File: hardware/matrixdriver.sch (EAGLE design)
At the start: 50 parts, among them IC1 75176AD, IC2 4017D, IC3 ULN2803, IC4 7805DT, Q1 20MHZ, Q2 MMBT4403LT1SMD, Q3 BC856, Q4 BC856, Q5 BC856, Q6 BC856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

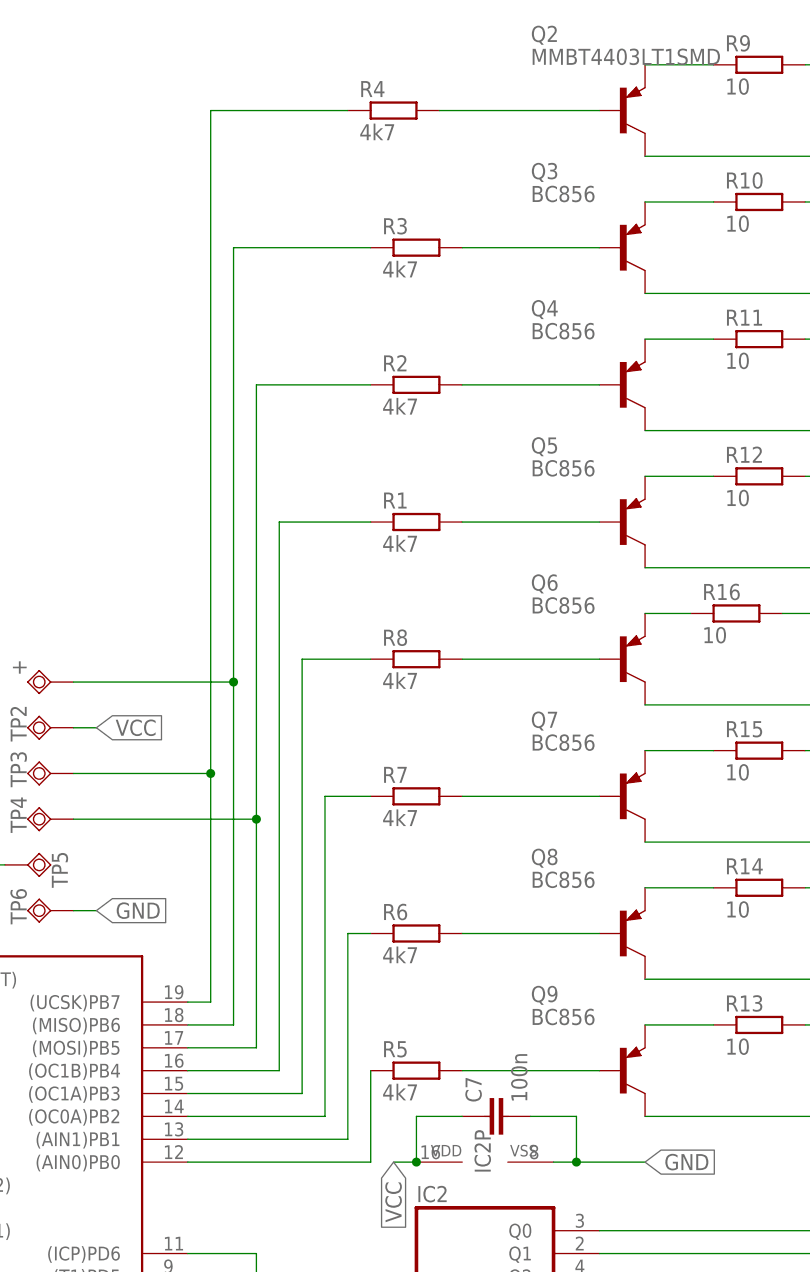
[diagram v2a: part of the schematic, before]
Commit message: board changes without resistor at base
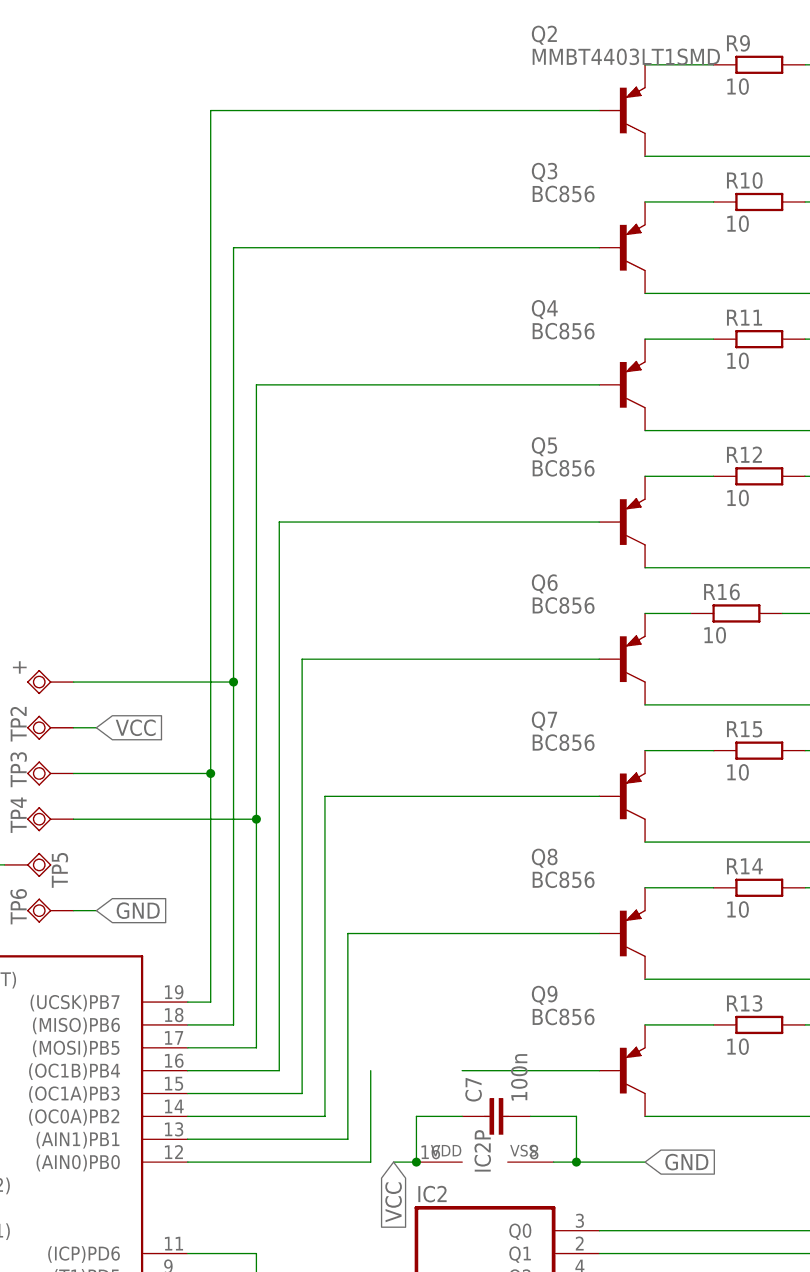
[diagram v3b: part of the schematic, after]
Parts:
- removed R1, R2, R3, R4, R5, R6, R7, R8: 4k7, resistor:R-EU_R1206
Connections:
- removed net N$37: Q2.B, R4.2
- removed net N$38: Q4.B, R2.2
- removed net N$39: Q5.B, R1.2
- removed net N$40: Q8.B, R6.2
- removed net N$42: Q6.B, R8.2
- removed net N$43: Q7.B, R7.2
- removed net N$7: +.TP, R3.1, U$1.(MISO)PB6
- net N$1: no longer R5.1
- net N$2: now also Q8.B; no longer R6.1
- net N$3: now also Q7.B; no longer R7.1
- net N$32: now also +.TP, U$1.(MISO)PB6; no longer R3.2
- net N$4: now also Q6.B; no longer R8.1
- net N$41: no longer R5.2
- net N$5: now also Q5.B; no longer R1.1
- net N$6: now also Q4.B; no longer R2.1
- net N$8: now also Q2.B; no longer R4.1
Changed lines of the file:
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@@
 <part name="Q1" library="crystal" deviceset="CRYSTAL" device="HC49UP" value="20MHZ"/>
 <part name="U$2" library="con-dc-jack" deviceset="CUI_PJ-102A" device=""/>
-<part name="R2" library="resistor" deviceset="R-EU_" device="R1206" value="4k7"/>
-<part name="R1" library="resistor" deviceset="R-EU_" device="R1206" value="4k7"/>
-<part name="R3" library="resistor" deviceset="R-EU_" device="R1206" value="4k7"/>
-<part name="R4" library="resistor" deviceset="R-EU_" device="R1206" value="4k7"/>
-<part name="R5" library="resistor" deviceset="R-EU_" device="R1206" value="4k7"/>
-<part name="R6" library="resistor" deviceset="R-EU_" device="R1206" value="4k7"/>
-<part name="R7" library="resistor" deviceset="R-EU_" device="R1206" value="4k7"/>
-<part name="R8" library="resistor" deviceset="R-EU_" device="R1206" value="4k7"/>
 <part name="R9" library="resistor" deviceset="R-EU_" device="R1206" value="10"/>
 <part name="R10" library="resistor" deviceset="R-EU_" device="R1206" value="10"/>
@@
 <instance part="Q1" gate="G$1" x="30.48" y="68.58" rot="R90"/>
 <instance part="U$2" gate="G$1" x="12.7" y="101.6" rot="R270"/>
-<instance part="R2" gate="G$1" x="101.6" y="160.02"/>
-<instance part="R1" gate="G$1" x="101.6" y="144.78"/>
-<instance part="R3" gate="G$1" x="101.6" y="175.26"/>
-<instance part="R4" gate="G$1" x="99.06" y="190.5"/>
-<instance part="R5" gate="G$1" x="101.6" y="83.82"/>
-<instance part="R6" gate="G$1" x="101.6" y="99.06"/>
-<instance part="R7" gate="G$1" x="101.6" y="114.3"/>
-<instance part="R8" gate="G$1" x="101.6" y="129.54"/>
 <instance part="R9" gate="G$1" x="139.7" y="195.58"/>
 <instance part="R10" gate="G$1" x="139.7" y="180.34"/>
@@
 <wire x1="76.2" y1="73.66" x2="96.52" y2="73.66" width="0.1524" layer="91"/>
 <wire x1="96.52" y1="73.66" x2="96.52" y2="83.82" width="0.1524" layer="91"/>
-<pinref part="R5" gate="G$1" pin="1"/>
 </segment>
 </net>
@@
 <wire x1="76.2" y1="76.2" x2="93.98" y2="76.2" width="0.1524" layer="91"/>
 <wire x1="93.98" y1="76.2" x2="93.98" y2="99.06" width="0.1524" layer="91"/>
-<wire x1="93.98" y1="99.06" x2="96.52" y2="99.06" width="0.1524" layer="91"/>
-<pinref part="R6" gate="G$1" pin="1"/>
+<pinref part="Q8" gate="G$1" pin="B"/>
+<wire x1="121.92" y1="99.06" x2="93.98" y2="99.06" width="0.1524" layer="91"/>
 </segment>
 </net>
@@
 <wire x1="76.2" y1="78.74" x2="91.44" y2="78.74" width="0.1524" layer="91"/>
 <wire x1="91.44" y1="78.74" x2="91.44" y2="114.3" width="0.1524" layer="91"/>
-<wire x1="91.44" y1="114.3" x2="96.52" y2="114.3" width="0.1524" layer="91"/>
-<pinref part="R7" gate="G$1" pin="1"/>
+<pinref part="Q7" gate="G$1" pin="B"/>
+<wire x1="91.44" y1="114.3" x2="121.92" y2="114.3" width="0.1524" layer="91"/>
 </segment>
 </net>
@@
 <wire x1="76.2" y1="81.28" x2="88.9" y2="81.28" width="0.1524" layer="91"/>
 <wire x1="88.9" y1="81.28" x2="88.9" y2="129.54" width="0.1524" layer="91"/>
-<wire x1="88.9" y1="129.54" x2="96.52" y2="129.54" width="0.1524" layer="91"/>
-<pinref part="R8" gate="G$1" pin="1"/>
+<pinref part="Q6" gate="G$1" pin="B"/>
+<wire x1="88.9" y1="129.54" x2="121.92" y2="129.54" width="0.1524" layer="91"/>
 </segment>
 </net>
@@
 <wire x1="76.2" y1="83.82" x2="86.36" y2="83.82" width="0.1524" layer="91"/>
 <wire x1="86.36" y1="83.82" x2="86.36" y2="144.78" width="0.1524" layer="91"/>
-<wire x1="86.36" y1="144.78" x2="96.52" y2="144.78" width="0.1524" layer="91"/>
-<pinref part="R1" gate="G$1" pin="1"/>
+<wire x1="86.36" y1="144.78" x2="121.92" y2="144.78" width="0.1524" layer="91"/>
+<pinref part="Q5" gate="G$1" pin="B"/>
 </segment>
 </net>
@@
 <wire x1="63.5" y1="111.76" x2="83.82" y2="111.76" width="0.1524" layer="91"/>
 <junction x="83.82" y="111.76"/>
-<wire x1="83.82" y1="160.02" x2="96.52" y2="160.02" width="0.1524" layer="91"/>
-<pinref part="R2" gate="G$1" pin="1"/>
-</segment>
-</net>
-<net name="N$7" class="0">
-<segment>
-<pinref part="U$1" gate="G$1" pin="(MISO)PB6"/>
-<wire x1="76.2" y1="88.9" x2="81.28" y2="88.9" width="0.1524" layer="91"/>
-<wire x1="81.28" y1="88.9" x2="81.28" y2="127" width="0.1524" layer="91"/>
-<wire x1="81.28" y1="127" x2="81.28" y2="175.26" width="0.1524" layer="91"/>
-<wire x1="81.28" y1="175.26" x2="96.52" y2="175.26" width="0.1524" layer="91"/>
-<pinref part="+" gate="G$1" pin="TP"/>
-<wire x1="63.5" y1="127" x2="81.28" y2="127" width="0.1524" layer="91"/>
-<junction x="81.28" y="127"/>
-<pinref part="R3" gate="G$1" pin="1"/>
+<wire x1="83.82" y1="160.02" x2="121.92" y2="160.02" width="0.1524" layer="91"/>
+<pinref part="Q4" gate="G$1" pin="B"/>
 </segment>
 </net>
@@
 <wire x1="78.74" y1="91.44" x2="78.74" y2="116.84" width="0.1524" layer="91"/>
 <wire x1="78.74" y1="116.84" x2="78.74" y2="190.5" width="0.1524" layer="91"/>
-<wire x1="78.74" y1="190.5" x2="93.98" y2="190.5" width="0.1524" layer="91"/>
+<wire x1="78.74" y1="190.5" x2="121.92" y2="190.5" width="0.1524" layer="91"/>
 <pinref part="TP3" gate="G$1" pin="TP"/>
 <wire x1="63.5" y1="116.84" x2="78.74" y2="116.84" width="0.1524" layer="91"/>
 <junction x="78.74" y="116.84"/>
-<pinref part="R4" gate="G$1" pin="1"/>
+<pinref part="Q2" gate="G$1" pin="B"/>
 </segment>
 </net>
@@
 </segment>
 </net>
-<net name="N$32" class="0">
-<segment>
-<pinref part="Q3" gate="G$1" pin="B"/>
-<wire x1="106.68" y1="175.26" x2="121.92" y2="175.26" width="0.1524" layer="91"/>
-<pinref part="R3" gate="G$1" pin="2"/>
-</segment>
-</net>
-<net name="N$37" class="0">
-<segment>
-<pinref part="Q2" gate="G$1" pin="B"/>
-<wire x1="104.14" y1="190.5" x2="121.92" y2="190.5" width="0.1524" layer="91"/>
-<pinref part="R4" gate="G$1" pin="2"/>
-</segment>
-</net>
-<net name="N$38" class="0">
-<segment>
-<pinref part="Q4" gate="G$1" pin="B"/>
-<wire x1="121.92" y1="160.02" x2="106.68" y2="160.02" width="0.1524" layer="91"/>
-<pinref part="R2" gate="G$1" pin="2"/>
-</segment>
-</net>
-<net name="N$39" class="0">
-<segment>
-<pinref part="Q5" gate="G$1" pin="B"/>
-<wire x1="121.92" y1="144.78" x2="106.68" y2="144.78" width="0.1524" layer="91"/>
-<pinref part="R1" gate="G$1" pin="2"/>
-</segment>
-</net>
-<net name="N$40" class="0">
-<segment>
-<pinref part="Q8" gate="G$1" pin="B"/>
-<wire x1="121.92" y1="99.06" x2="106.68" y2="99.06" width="0.1524" layer="91"/>
-<pinref part="R6" gate="G$1" pin="2"/>
-</segment>
-</net>
 <net name="N$41" class="0">
 <segment>
 <pinref part="Q9" gate="G$1" pin="B"/>
 <wire x1="121.92" y1="83.82" x2="106.68" y2="83.82" width="0.1524" layer="91"/>
-<pinref part="R5" gate="G$1" pin="2"/>
-</segment>
-</net>
-<net name="N$42" class="0">
-<segment>
-<pinref part="Q6" gate="G$1" pin="B"/>
-<wire x1="106.68" y1="129.54" x2="121.92" y2="129.54" width="0.1524" layer="91"/>
-<pinref part="R8" gate="G$1" pin="2"/>
-</segment>
-</net>
-<net name="N$43" class="0">
-<segment>
-<wire x1="106.68" y1="114.3" x2="121.92" y2="114.3" width="0.1524" layer="91"/>
-<pinref part="Q7" gate="G$1" pin="B"/>
-<pinref part="R7" gate="G$1" pin="2"/>
 </segment>
 </net>
@@
 </segment>
 </net>
+<net name="N$32" class="0">
+<segment>
+<pinref part="U$1" gate="G$1" pin="(MISO)PB6"/>
+<wire x1="76.2" y1="88.9" x2="81.28" y2="88.9" width="0.1524" layer="91"/>
+<wire x1="81.28" y1="88.9" x2="81.28" y2="127" width="0.1524" layer="91"/>
+<wire x1="81.28" y1="127" x2="81.28" y2="175.26" width="0.1524" layer="91"/>
+<wire x1="81.28" y1="175.26" x2="121.92" y2="175.26" width="0.1524" layer="91"/>
+<pinref part="+" gate="G$1" pin="TP"/>
+<wire x1="63.5" y1="127" x2="81.28" y2="127" width="0.1524" layer="91"/>
+<junction x="81.28" y="127"/>
+<pinref part="Q3" gate="G$1" pin="B"/>
+</segment>
+</net>
